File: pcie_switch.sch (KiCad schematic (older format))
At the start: 52 parts, among them J4 Conn_01x03_Male, U2 PI7C9X2G404SL

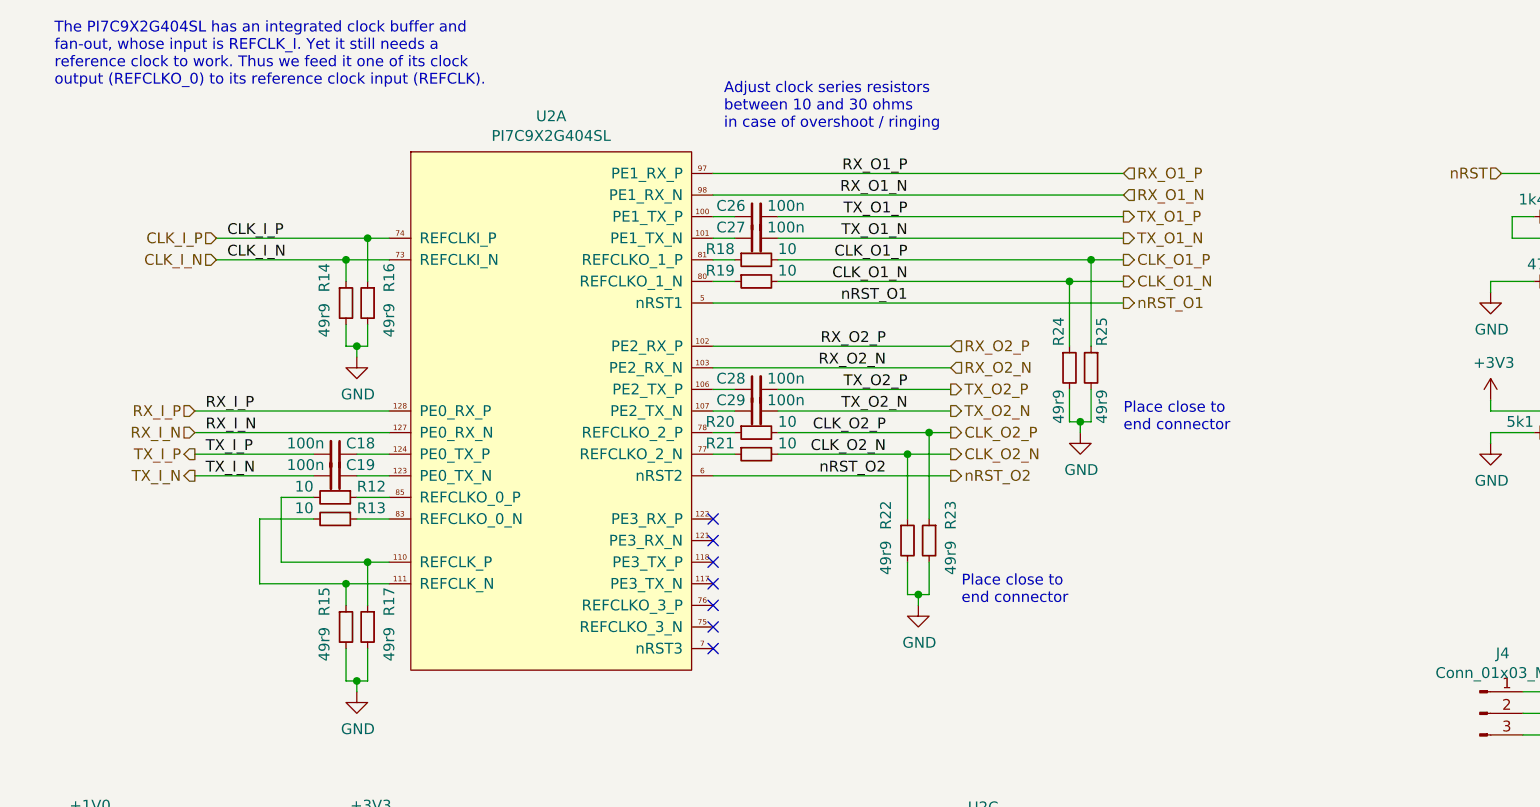
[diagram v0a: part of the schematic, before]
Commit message: sch: Add missing differential net names
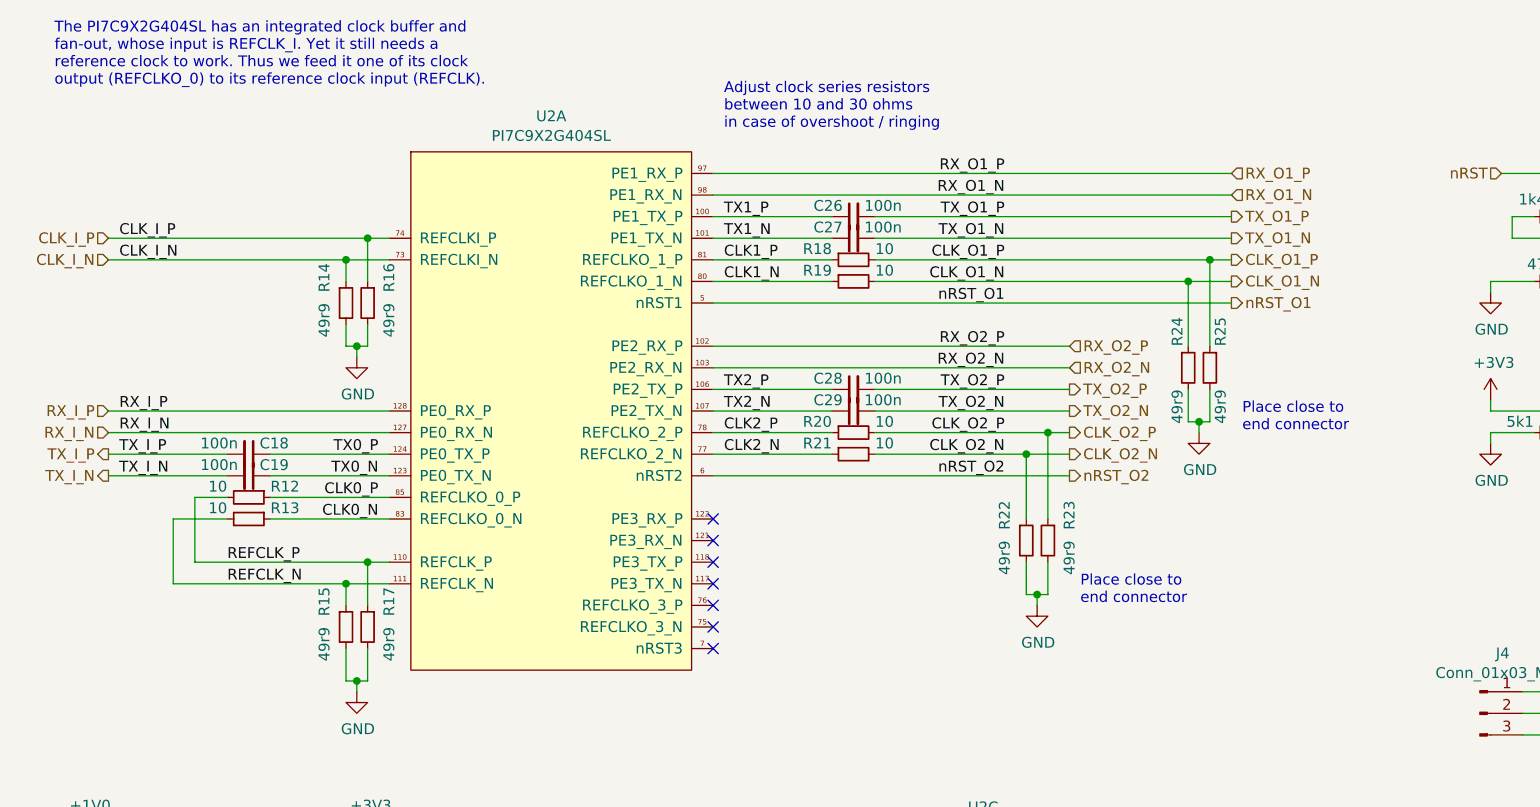
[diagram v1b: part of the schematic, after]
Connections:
- net CLK0_P: now reaches R12.1, U2.85 (REFCLKO_0_P)
- net REFCLK_P: now reaches R12.2, R17.1, U2.110 (REFCLK_P)
- net CLK0_N: now reaches R13.1, U2.83 (REFCLKO_0_N)
- net REFCLK_N: now reaches R13.2, R15.1, U2.111 (REFCLK_N)
- net TX1_P: now reaches C26.1, U2.100 (PE1_TX_P)
- net TX1_N: now reaches C27.1, U2.101 (PE1_TX_N)
- net TX2_P: now reaches C28.1, U2.106 (PE2_TX_P)
- net TX2_N: now reaches C29.1, U2.107 (PE2_TX_N)
- net TX0_N: now reaches C19.1, U2.123 (PE0_TX_N)
- net TX0_P: now reaches C18.1, U2.124 (PE0_TX_P)
- net CLK2_N: now reaches R21.1, U2.77 (REFCLKO_2_N)
- net CLK2_P: now reaches R20.1, U2.78 (REFCLKO_2_P)
- net CLK1_N: now reaches R19.1, U2.80 (REFCLKO_1_N)
- net CLK1_P: now reaches R18.1, U2.81 (REFCLKO_1_P)
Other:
- moved on the sheet: C18, C19, C26, C27, C28, C29, R12, R13, R18, R19, R20, R21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

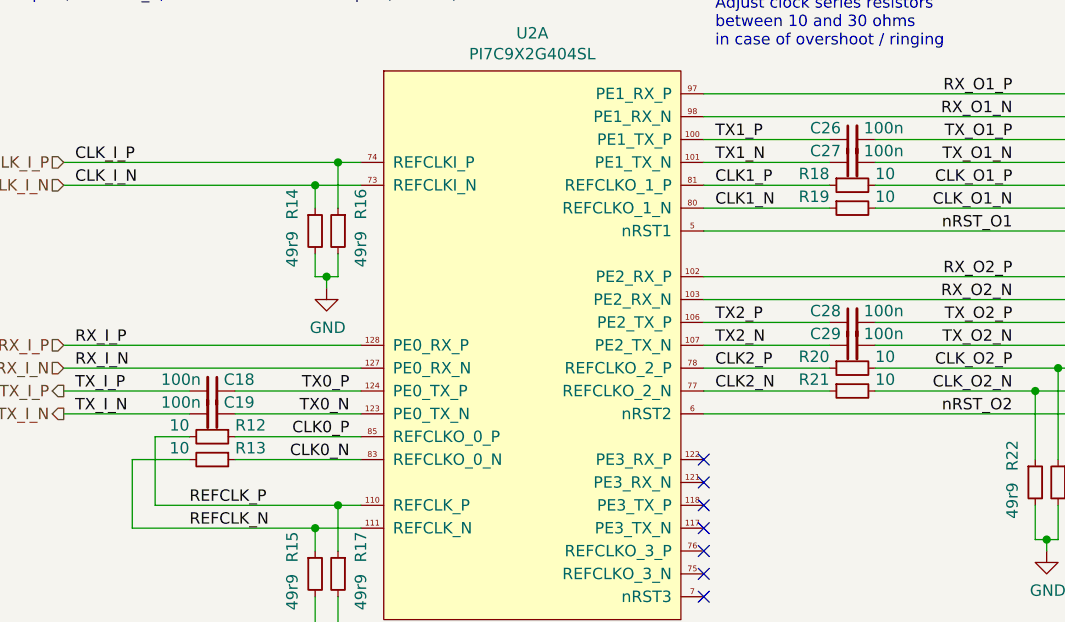
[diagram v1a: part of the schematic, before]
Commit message: sch: Change PCIe series resistors to 33 ohm
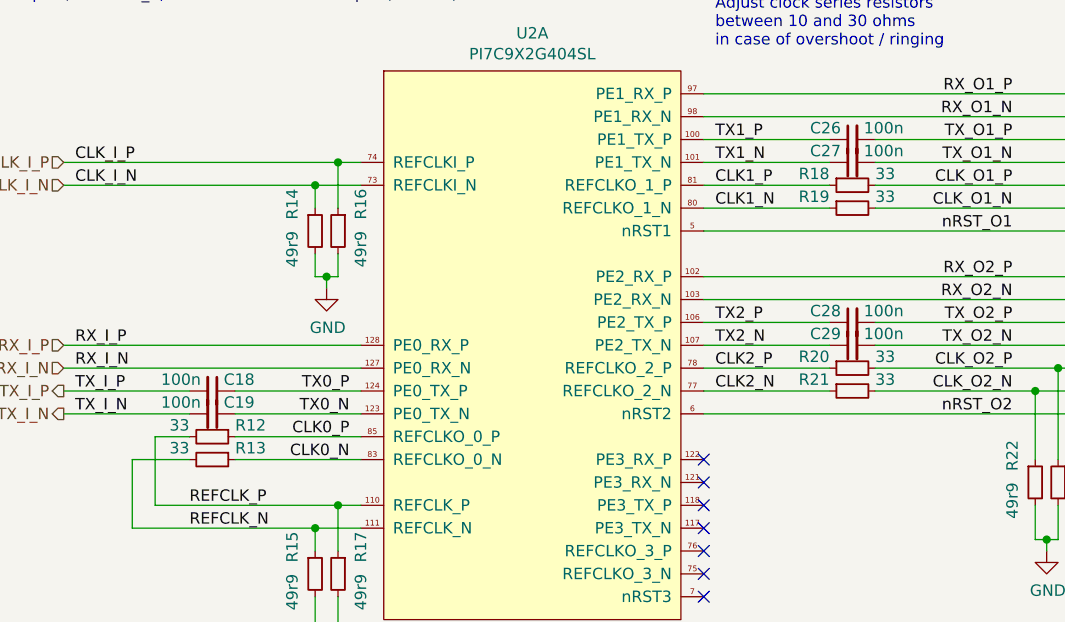
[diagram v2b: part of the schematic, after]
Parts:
- R12, R13, R18, R19, R20, R21: value 10 -> 33
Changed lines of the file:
@@
 P 4450 2700
 F 0 "R20" V 4400 2800 50  0000 L CNN
-F 1 "10" V 4400 2600 50  0000 R CNN
+F 1 "33" V 4400 2600 50  0000 R CNN
 F 2 "Resistor_SMD:R_0402_1005Metric" H 4450 2700 50  0001 C CNN
 F 3 "~" H 4450 2700 50  0001 C CNN
@@
 P 4450 2800
 F 0 "R21" V 4400 2900 50  0000 L CNN
-F 1 "10" V 4400 2700 50  0000 R CNN
+F 1 "33" V 4400 2700 50  0000 R CNN
 F 2 "Resistor_SMD:R_0402_1005Metric" H 4450 2800 50  0001 C CNN
 F 3 "~" H 4450 2800 50  0001 C CNN
@@
 P 1650 3000
 F 0 "R12" V 1600 3100 50  0000 L CNN
-F 1 "10" V 1600 2900 50  0000 R CNN
+F 1 "33" V 1600 2900 50  0000 R CNN
 F 2 "Resistor_SMD:R_0402_1005Metric" H 1650 3000 50  0001 C CNN
 F 3 "~" H 1650 3000 50  0001 C CNN
@@
 P 1650 3100
 F 0 "R13" V 1600 3200 50  0000 L CNN
-F 1 "10" V 1600 3000 50  0000 R CNN
+F 1 "33" V 1600 3000 50  0000 R CNN
 F 2 "Resistor_SMD:R_0402_1005Metric" H 1650 3100 50  0001 C CNN
 F 3 "~" H 1650 3100 50  0001 C CNN
@@
 P 4450 1900
 F 0 "R18" V 4400 2000 50  0000 L CNN
-F 1 "10" V 4400 1800 50  0000 R CNN
+F 1 "33" V 4400 1800 50  0000 R CNN
 F 2 "Resistor_SMD:R_0402_1005Metric" H 4450 1900 50  0001 C CNN
 F 3 "~" H 4450 1900 50  0001 C CNN
@@
 P 4450 2000
 F 0 "R19" V 4400 2100 50  0000 L CNN
-F 1 "10" V 4400 1900 50  0000 R CNN
+F 1 "33" V 4400 1900 50  0000 R CNN
 F 2 "Resistor_SMD:R_0402_1005Metric" H 4450 2000 50  0001 C CNN
 F 3 "~" H 4450 2000 50  0001 C CNN

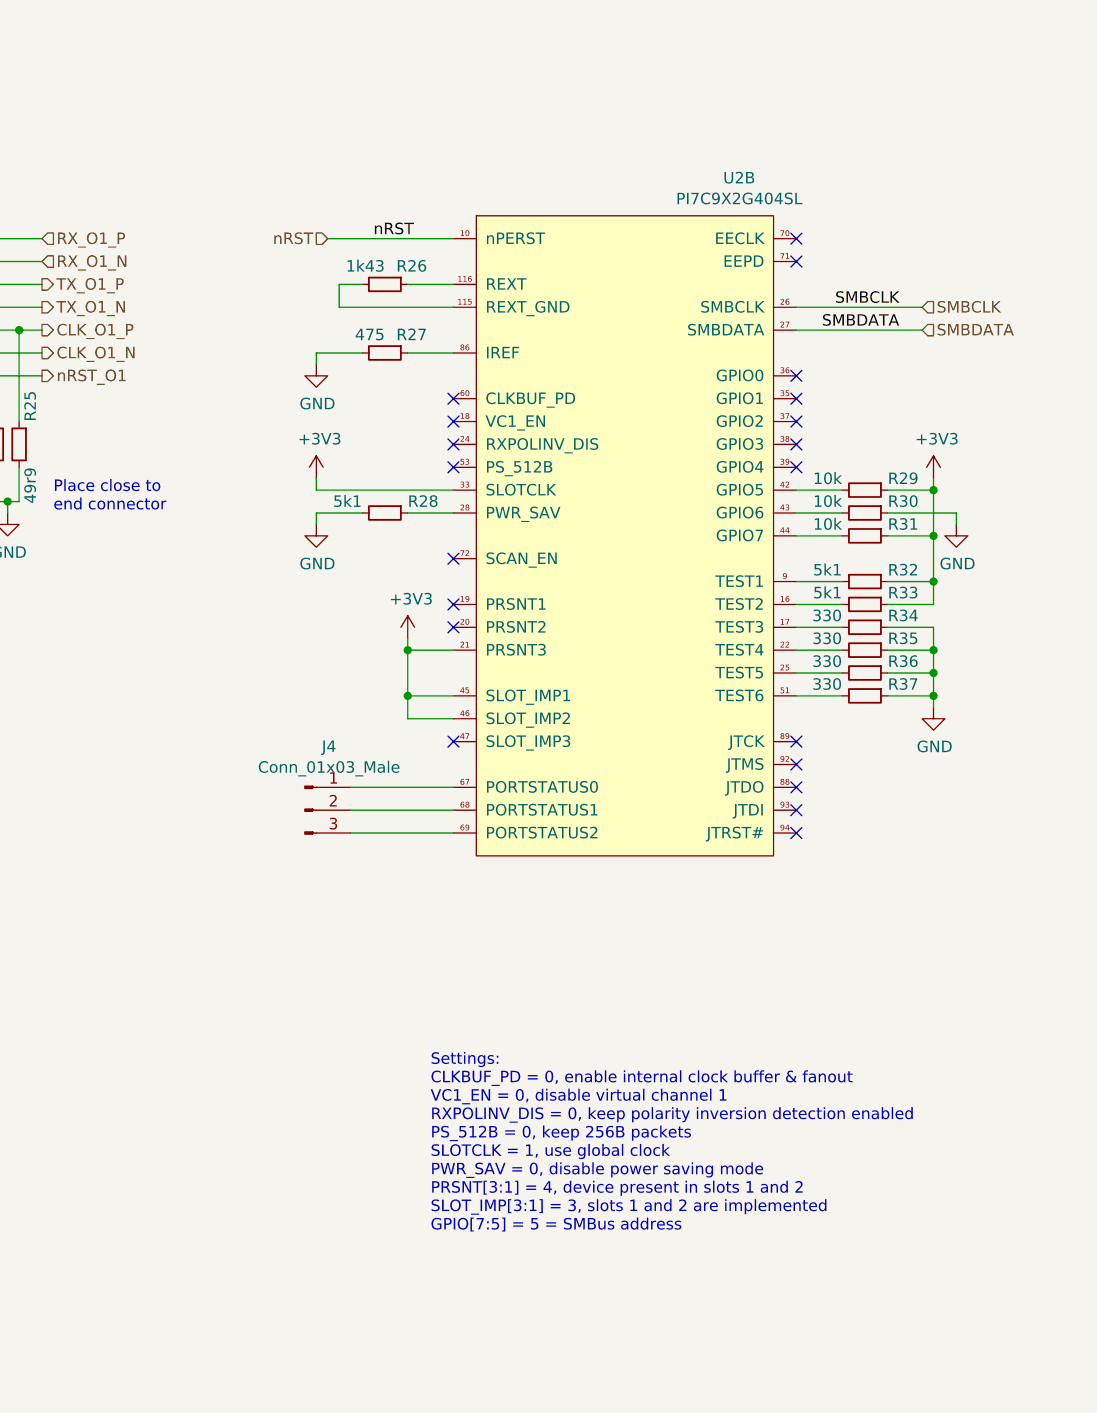
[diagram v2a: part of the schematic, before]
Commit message: sch: Add missing decoupling caps for PCIe switch
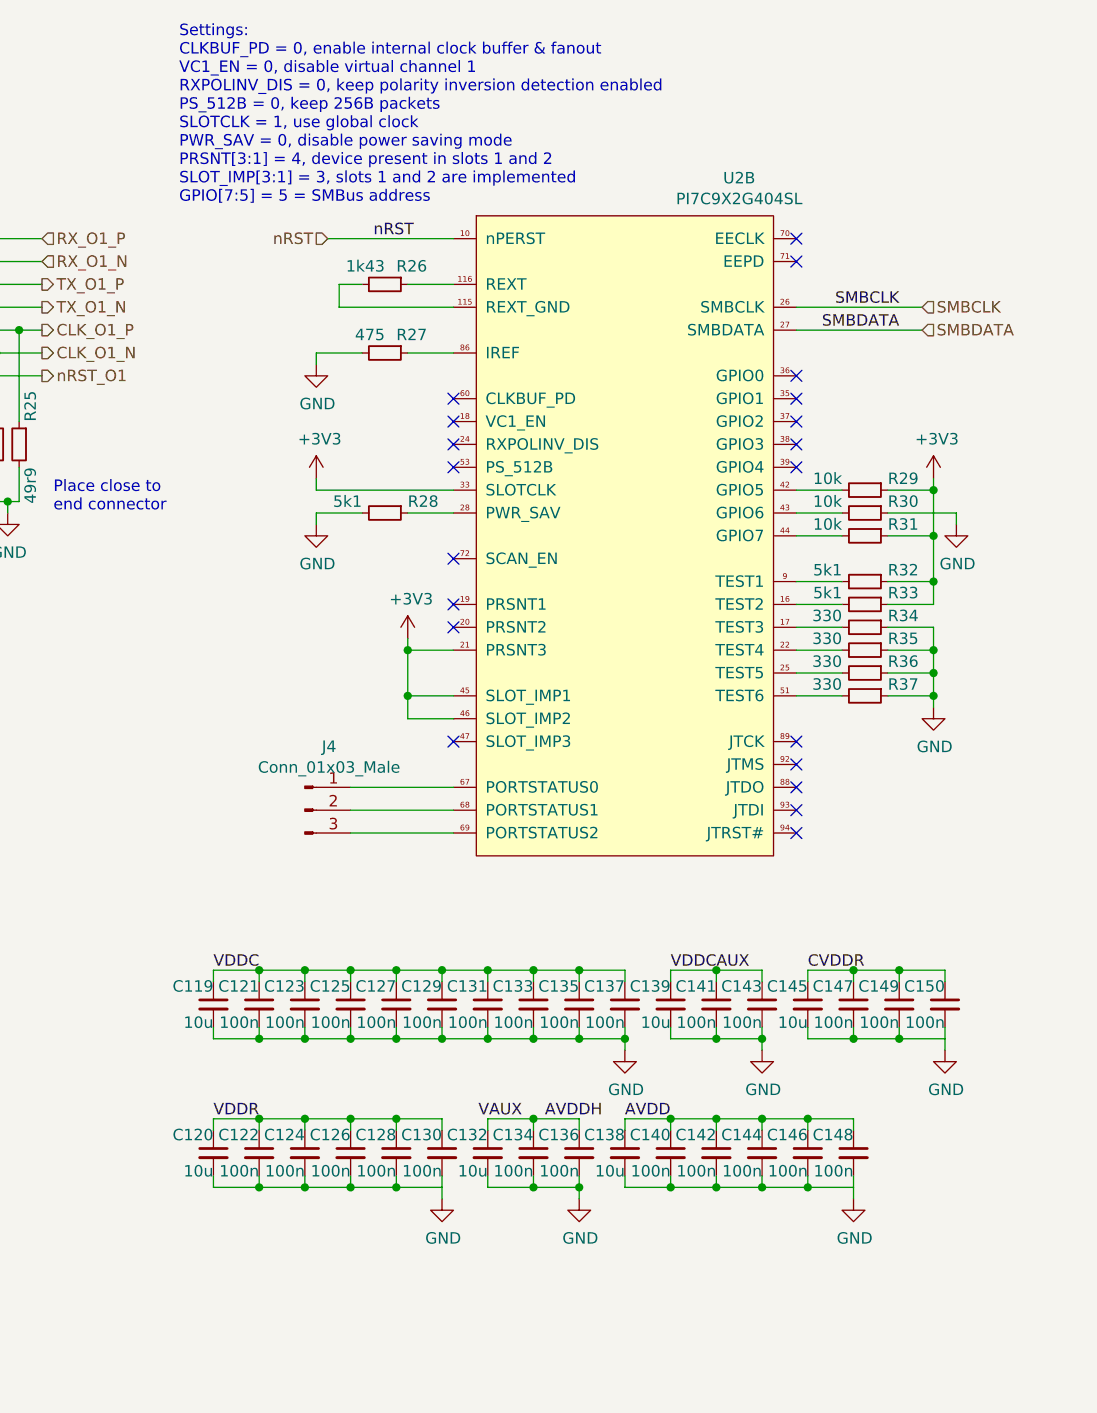
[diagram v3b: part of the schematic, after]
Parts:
- added C119, C120, C132, C138, C139, C145: 10u, Capacitor_SMD:C_0603_1608Metric, symbol Device:C_Small
- added C121, C122, C123, C124, C125, C126, C127, C128, C129, C130, C131, C133, C134, C135, C136, C137, C140, C141, C142, C143, C144, C146, C147, C148, C149, C150: 100n, Capacitor_SMD:C_0603_1608Metric, symbol Device:C_Small
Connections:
- net AVDD: now also C138.1, C140.1, C142.1, C144.1, C146.1, C148.1
- net AVDDH: now also C132.1, C134.1, C136.1
- net CVDDR: now also C145.1, C147.1, C149.1, C150.1
- net GND: now also C119.2, C120.2, C121.2, C122.2, C123.2, C124.2, C125.2, C126.2, C127.2, C128.2, C129.2, C130.2, C131.2, C132.2, C133.2, C134.2, C135.2, C136.2, C137.2, C138.2, C139.2, C140.2, C141.2, C142.2, C143.2, C144.2, C145.2, C146.2, C147.2, C148.2, C149.2, C150.2
- net VDDC: now also C119.1, C121.1, C123.1, C125.1, C127.1, C129.1, C131.1, C133.1, C135.1, C137.1
- net VDDCAUX: now also C139.1, C141.1, C143.1
- net VDDR: now also C120.1, C122.1, C124.1, C126.1, C128.1, C130.1

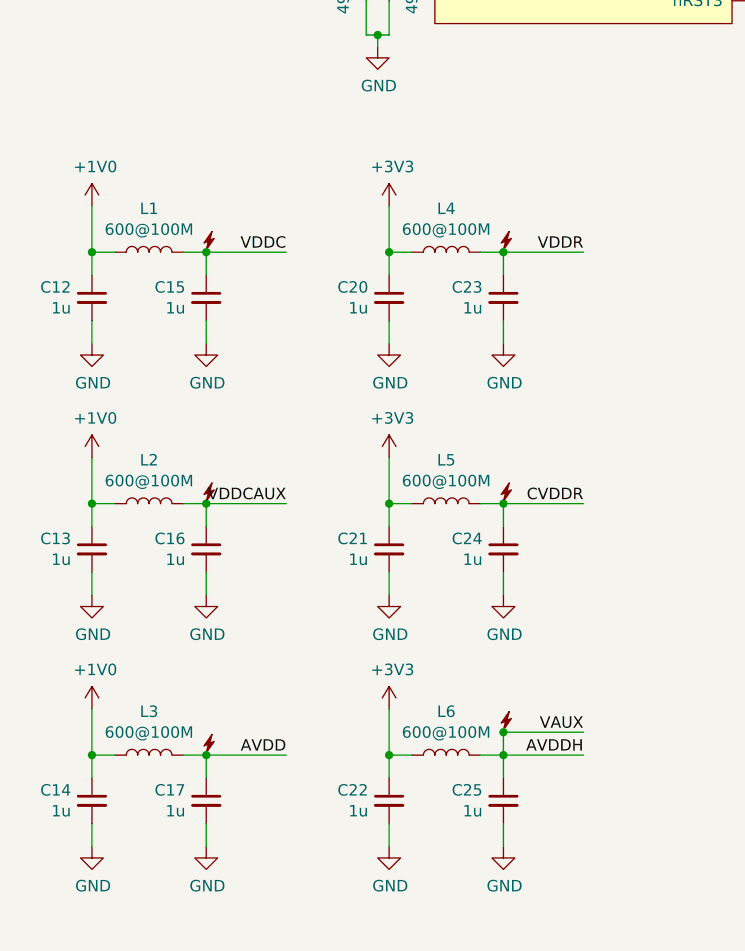
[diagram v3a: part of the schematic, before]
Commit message: sch: Simplify PSU
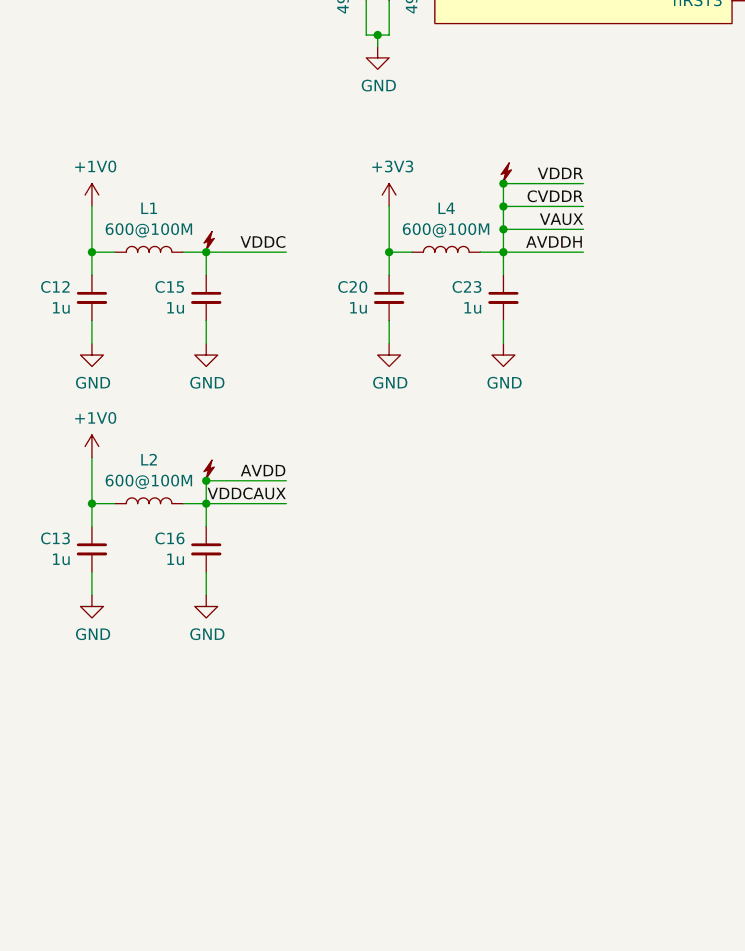
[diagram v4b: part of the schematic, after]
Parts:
- removed C14, C17, C21, C22, C24, C25: 1u, Capacitor_SMD:C_0603_1608Metric, symbol Device:C_Small
- removed L3, L5, L6: 600@100M, Inductor_SMD:L_0603_1608Metric, symbol Device:L
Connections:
- net CVDDR is gone; now on net AVDDH: C145.1, C147.1, C149.1, C150.1, U2.79 (CVDDR), U2.82 (CVDDR), U2.84 (CVDDR)
- net VDDCAUX is gone; now on net AVDD: C139.1, C141.1, C143.1, C16.1, L2.2, U2.13 (VDDCAUX), U2.14 (VDDCAUX)
- net VDDR is gone; now on net AVDDH: C120.1, C122.1, C124.1, C126.1, C128.1, C130.1, C23.1, L4.2, U2.1 (VDDR), U2.49 (VDDR), U2.64 (VDDR), U2.8 (VDDR), U2.96 (VDDR)
